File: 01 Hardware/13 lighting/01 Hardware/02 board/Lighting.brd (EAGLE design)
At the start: 69 x 80 mm, 58 parts, among them IC1 AD822R, IC2 AD822R, J2 614105150721, J3 690367290476, J4 690367291276, U10 Grün, U11 Rot, U7 W1, U8 W2

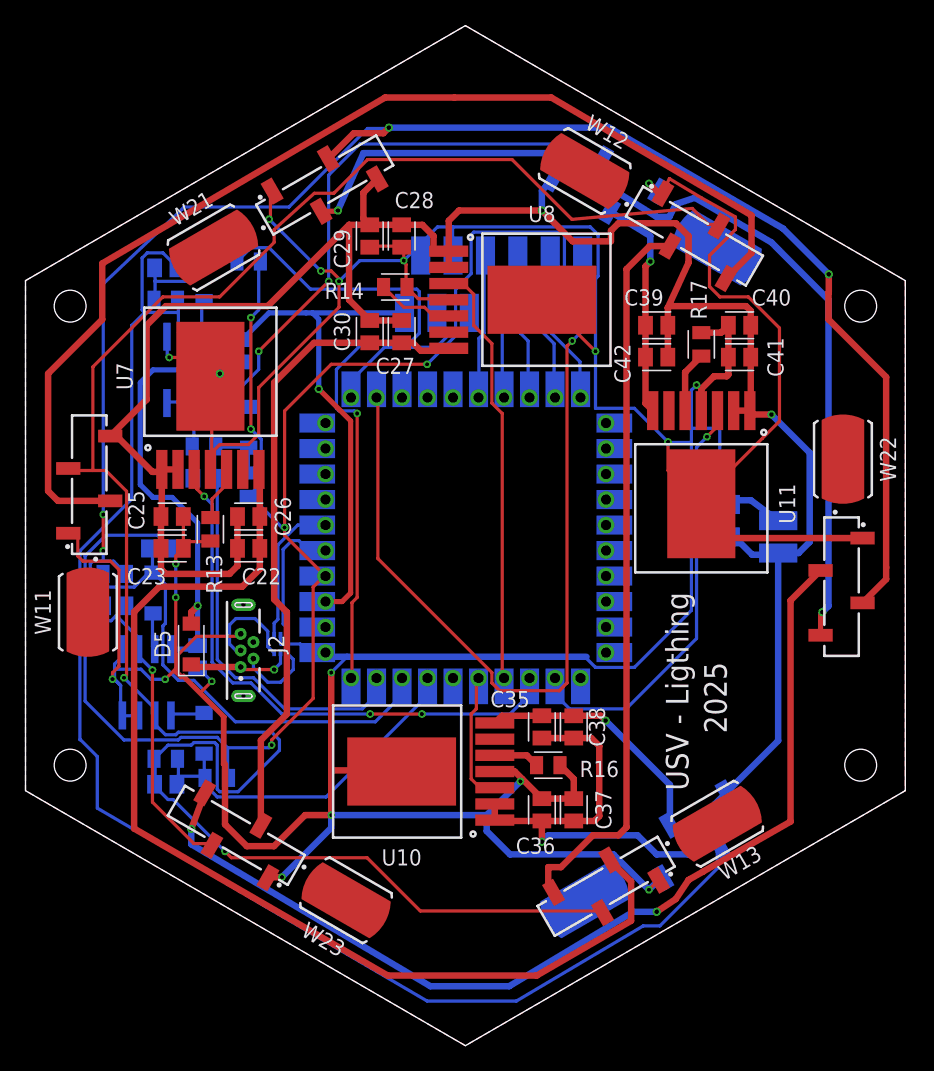
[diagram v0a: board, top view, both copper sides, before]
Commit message: new Pinlayout (LED-Board)
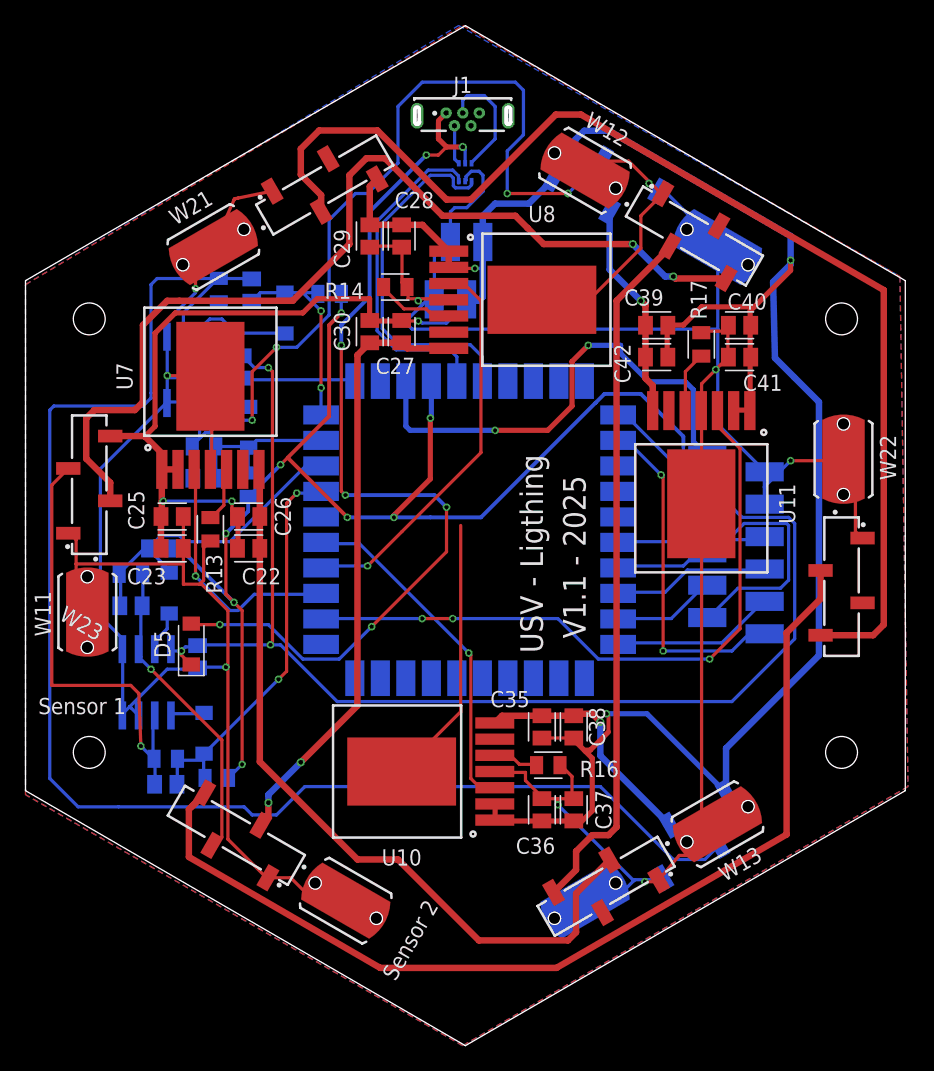
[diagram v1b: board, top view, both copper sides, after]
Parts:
- removed J2: 614105150721, Eagle_WR-USB (rev24c):614105150721
- added J1: 614105150621, Eagle_WR-USB (rev25c):614105150621
- GRUEN: value (none) -> GRUEN
- ROT: value (none) -> ROT
- U$1: value RP2350_STAMPTHT -> RP2350_STAMPSMD; device rp2xxx_stamp:RP2XXX_STAMP_TH -> rp2xxx_stamp:RP2XXX_STAMP_SMD
- W11: value (none) -> W11
- W12: value (none) -> W12
- W13: value (none) -> W13
- W21: value (none) -> W21
- W22: value (none) -> W22
- W23: value (none) -> W23
- moved D3 39.7 mm to (34.5, 68.5), turned to 0 degrees
- moved J3 30.5 mm to (34.0, 60.8), turned to 180 degrees
- moved J4 27.9 mm to (55.7, 39.3), turned to 90 degrees
- moved C5 6.96 mm to (17.7, 59.3), turned to 270 degrees
- moved D2 6.84 mm to (20.4, 57.5)
- moved R8 6.84 mm to (23.9, 59.0)
- moved R7 4.23 mm to (15.2, 59.3), turned to 90 degrees
- moved C6 1.27 mm to (17.0, 53.2)
- moved C2 1.27 mm to (8.27, 34.5)
- moved D8 1.27 mm to (11.3, 35.5)
- moved R3 1.27 mm to (8.27, 37.0)
- moved U$1 0.71 mm to (34.8, 40.5), turned to 0 degrees
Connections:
- net +3V3: no longer U$1.TH34
- net +5V: now also D5.1; no longer D5.2, U$1.TH33
- net ADC0: no longer U$1.TH27
- net ADC1: no longer U$1.TH28
- net ADC2: no longer U$1.TH29
- net ADC3: no longer U$1.TH30
- net D+@1: now also J1.3; no longer J2.3
- net D-@1: now also J1.2; no longer J2.2
- net D_N: no longer U$1.TH35
- net D_P: no longer U$1.TH36
- net GND: now also GRUEN.5, J1.5, J1.S1, J1.S2, ROT.5, W11.5, W12.5, W13.5, W21.5, W22.5, W23.5; no longer J2.5, U$1.TH31
- net N$11: no longer U$1.TH8
- net N$12: no longer U$1.TH7
- net N$14: no longer U$1.TH6
- net N$21: no longer U$1.TH2
- net N$22: no longer U$1.TH1
- net N$4: no longer U$1.TH10
- net N$6: no longer U$1.TH9
- net PD_W1: no longer W12.4, W13.4
- net PD_W2: no longer W21.4, W22.4
- net PWM_G: no longer U$1.TH22
- net PWM_R: no longer U$1.TH25
- net PWM_W1: no longer U$1.TH23
- net PWM_W2: no longer U$1.TH24
- net VBAT: no longer U$1.TH32
- net VBUS: now also D5.2, J1.1; no longer D5.1, J2.1
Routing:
- net PD_W2: track 154.2 -> 25.7 mm, vias 5 -> 1
- net PD_W1: track 159.7 -> 35.8 mm, vias 2 -> 1
- net VBUS: track 8.17 -> 73.7 mm, vias 1 -> 7
- net +5V: track 77.5 -> 140.3 mm, vias 2 -> 5
- net GND: track 417.9 -> 363.7 mm, vias 20 -> 9
- net ADC3: track 63.6 -> 18.3 mm, vias 1 -> 2
- net N$21: track 67.3 -> 26.9 mm, vias 1 -> 2
- net PWM_W1: track 44.3 -> 20.0 mm, vias 3 -> 1
- net ADC2: track 37.4 -> 13.1 mm
- net LED-W1-: track 84.8 -> 60.6 mm
- net PWM_G: track 33.8 -> 53.0 mm, vias 1 -> 3
- net W21_W22: track 74.3 -> 92.1 mm, vias 2 -> 0
- net D_P: track 11.6 -> 29.0 mm
- net PD_R: track 52.9 -> 69.9 mm, vias 2 -> 4
- net PWM_R: track 11.0 -> 27.2 mm, vias 0 -> 1
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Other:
- board text added: "Sensor 1"
- board text added: "Sensor 2"
- board text added: "V1.1 - 2025"
- board text removed: "2025"
